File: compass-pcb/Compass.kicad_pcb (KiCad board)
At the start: 2 copper layers, 18 parts

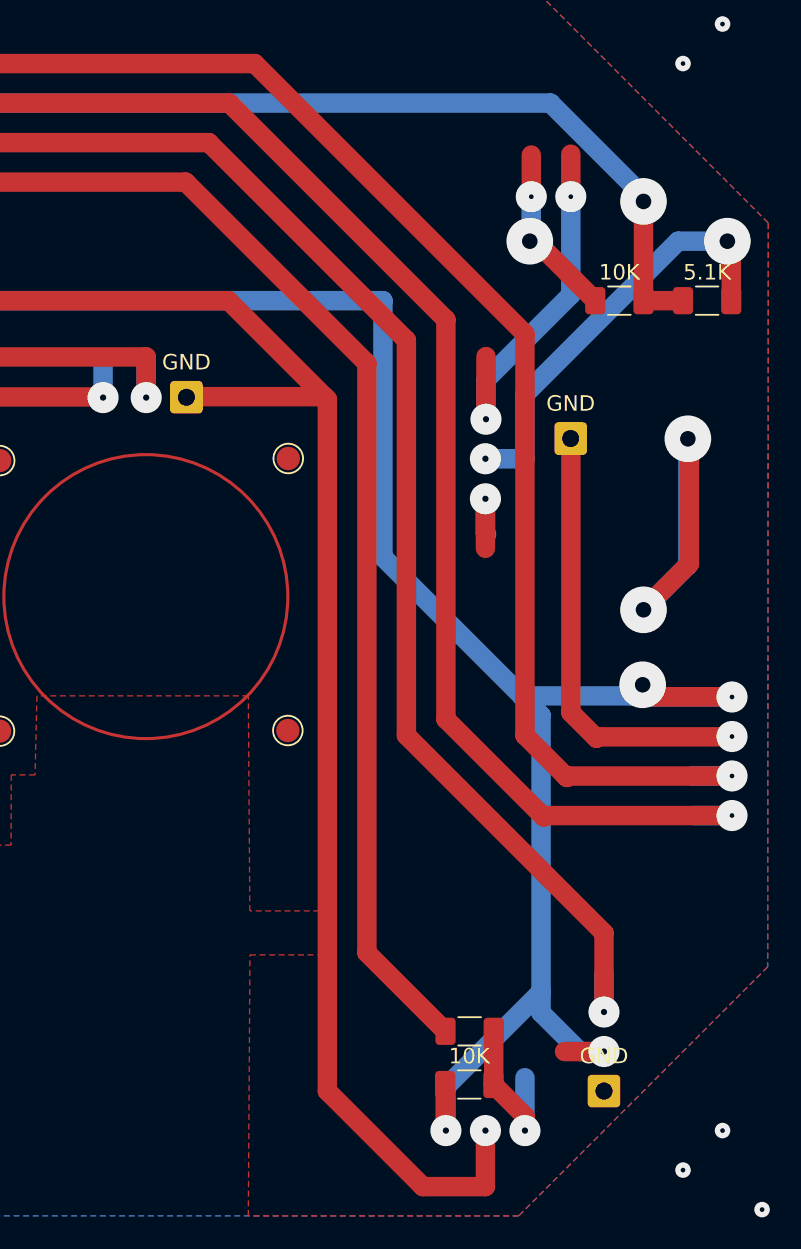
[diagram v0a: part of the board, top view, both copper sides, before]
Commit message: moving jumpers for more space
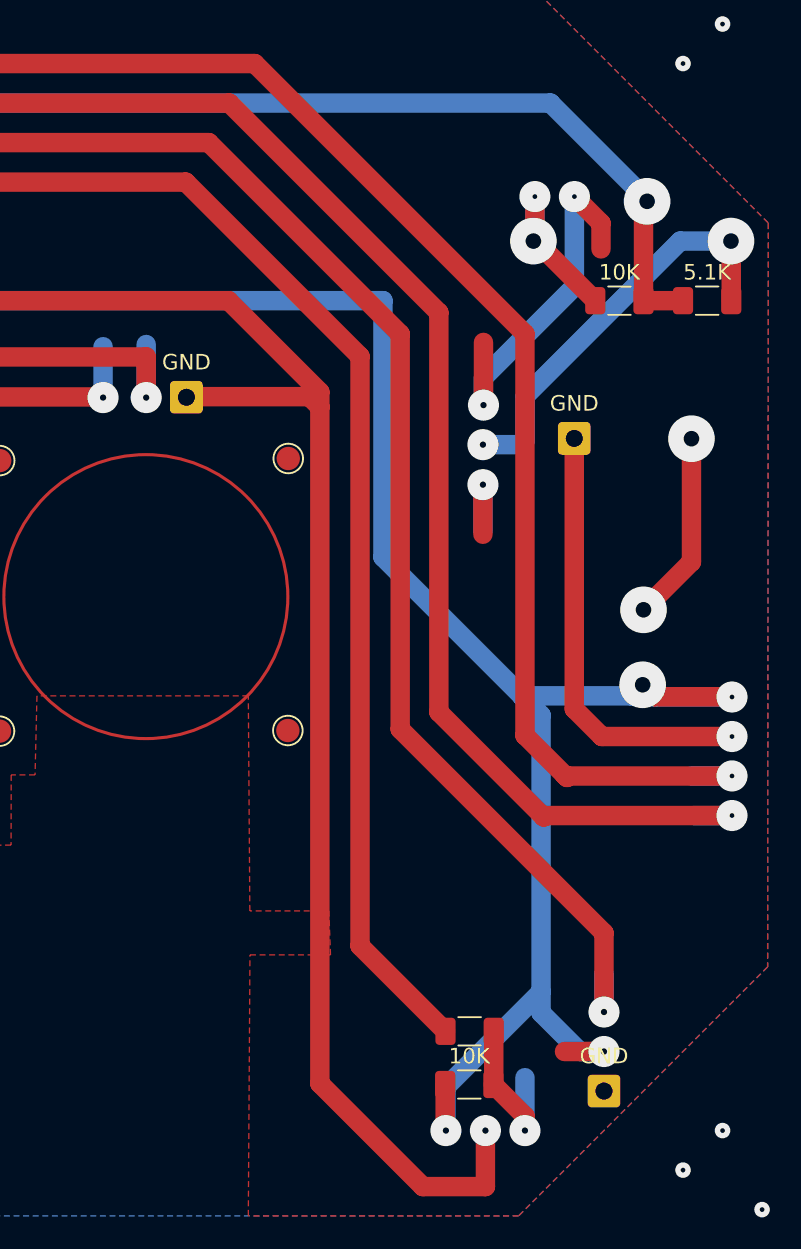
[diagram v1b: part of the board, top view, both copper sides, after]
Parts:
- moved GND 0.23 mm to (174.9, 83.8)
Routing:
- net (no net): track 1122.2 -> 1116.1 mm

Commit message: polishing
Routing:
- net (no net): track 1116.1 -> 1124.7 mm
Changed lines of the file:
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@@
   (segment (start 162.56 91.44) (end 162.56 74.958533) (width 1.25) (layer "B.Cu") (net 0))
   (segment (start 174.864516 68.268417) (end 174.864516 74.055484) (width 1.25) (layer "B.Cu") (net 0))
+  (segment (start 128.505445 100.278533) (end 130.516888 100.278533) (width 1.25) (layer "B.Cu") (net 0))
   (segment (start 108.787292 77.48937) (end 111.429859 77.48937) (width 1.25) (layer "B.Cu") (net 0))
   (segment (start 179.250238 99.646343) (end 178.538048 100.358533) (width 1.25) (layer "B.Cu") (net 0))
@@
   (segment (start 179.537067 68.472794) (end 173.322806 62.258533) (width 1.25) (layer "B.Cu") (net 0))
   (segment (start 108.85939 87.721468) (end 108.787292 87.64937) (width 1.25) (layer "B.Cu") (net 0))
+  (segment (start 168.984917 86.784602) (end 168.984917 89.944634) (width 1.25) (layer "B.Cu") (net 0))
   (segment (start 116.84 85.118533) (end 124.013168 85.118533) (width 1.25) (layer "B.Cu") (net 0))
   (segment (start 180.034912 100.431017) (end 184.993201 100.431017) (width 1.25) (layer "B.Cu") (net 0))
   (segment (start 121.473069 105.420339) (end 124.029538 105.420339) (width 1.25) (layer "B.Cu") (net 0))
   (segment (start 111.312994 79.999811) (end 108.816851 79.999811) (width 1.25) (layer "B.Cu") (net 0))
-  (segment (start 168.984917 86.784602) (end 168.984917 89.76346) (width 1.25) (layer "B.Cu") (net 0))
   (segment (start 168.984917 84.211715) (end 168.984917 83.90582) (width 1.25) (layer "B.Cu") (net 0))
   (segment (start 178.538048 100.358533) (end 171.478533 100.358533) (width 1.25) (layer "B.Cu") (net 0))
   (segment (start 108.818788 92.760866) (end 108.787292 92.72937) (width 1.25) (layer "B.Cu") (net 0))
+  (segment (start 128.505445 97.778533) (end 130.657549 97.778533) (width 1.25) (layer "B.Cu") (net 0))
   (segment (start 179.537067 68.573184) (end 179.537067 68.472794) (width 1.25) (layer "B.Cu") (net 0))
   (segment (start 171.69707 81.098057) (end 171.69707 83.966348) (width 1.25) (layer "B.Cu") (net 0))
@@
   (segment (start 123.96871 90.241167) (end 124.053119 90.156758) (width 1.25) (layer "B.Cu") (net 0))
   (segment (start 123.970383 110.561318) (end 124.013168 110.518533) (width 1.25) (layer "B.Cu") (net 0))
+  (segment (start 128.505445 102.898533) (end 130.678141 102.898533) (width 1.25) (layer "B.Cu") (net 0))
   (segment (start 166.605445 125.494555) (end 172.72 119.38) (width 1.25) (layer "B.Cu") (net 0))
   (segment (start 171.478533 100.358533) (end 172.72 101.6) (width 1.25) (layer "B.Cu") (net 0))
@@
   (segment (start 111.443824 100.34937) (end 111.453019 100.340175) (width 1.25) (layer "B.Cu") (net 0))
   (segment (start 179.250238 99.646343) (end 180.034912 100.431017) (width 1.25) (layer "B.Cu") (net 0))
+  (segment (start 128.505445 95.278533) (end 130.598297 95.278533) (width 1.25) (layer "B.Cu") (net 0))
   (segment (start 108.816851 82.539811) (end 108.787292 82.56937) (width 1.25) (layer "B.Cu") (net 0))
   (segment (start 124.053119 87.616758) (end 121.324313 87.616758) (width 1.25) (layer "B.Cu") (net 0))

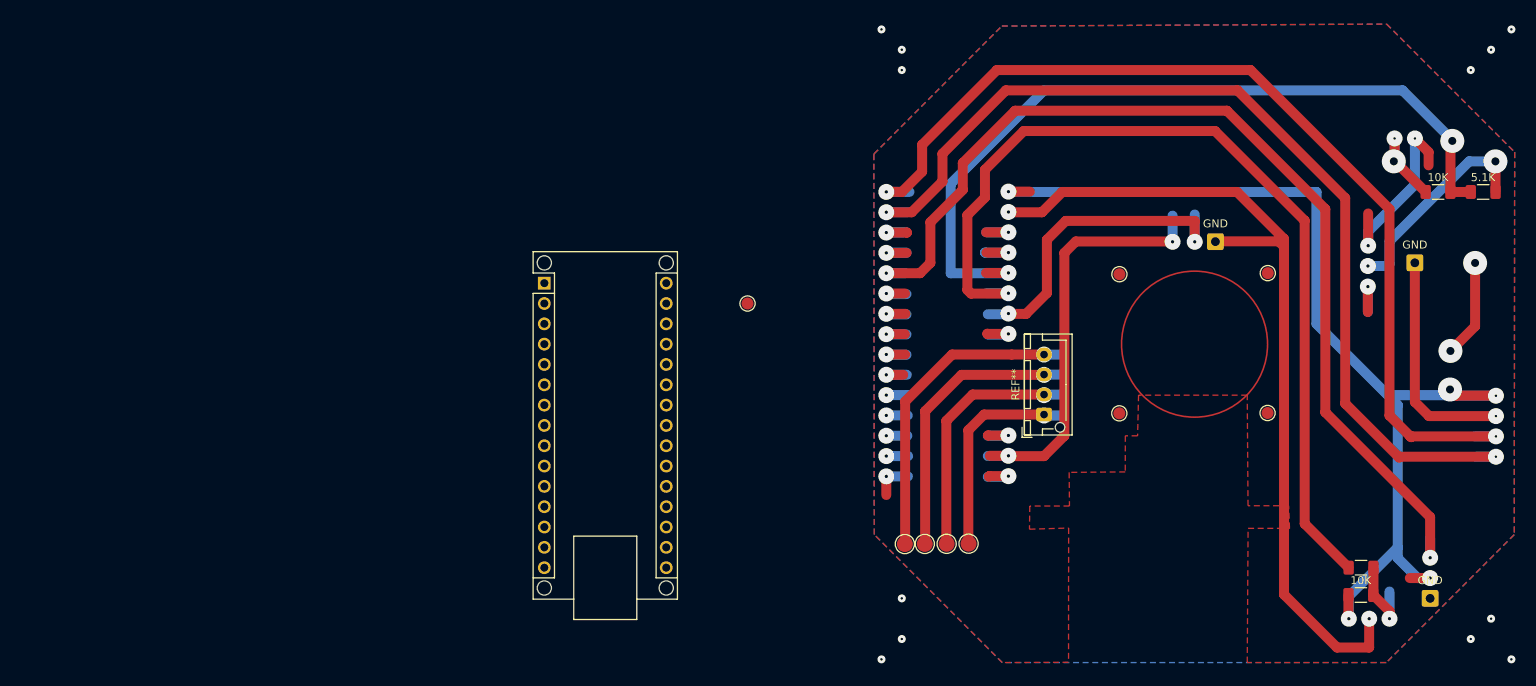
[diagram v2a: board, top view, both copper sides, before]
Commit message: moving main switch to the board
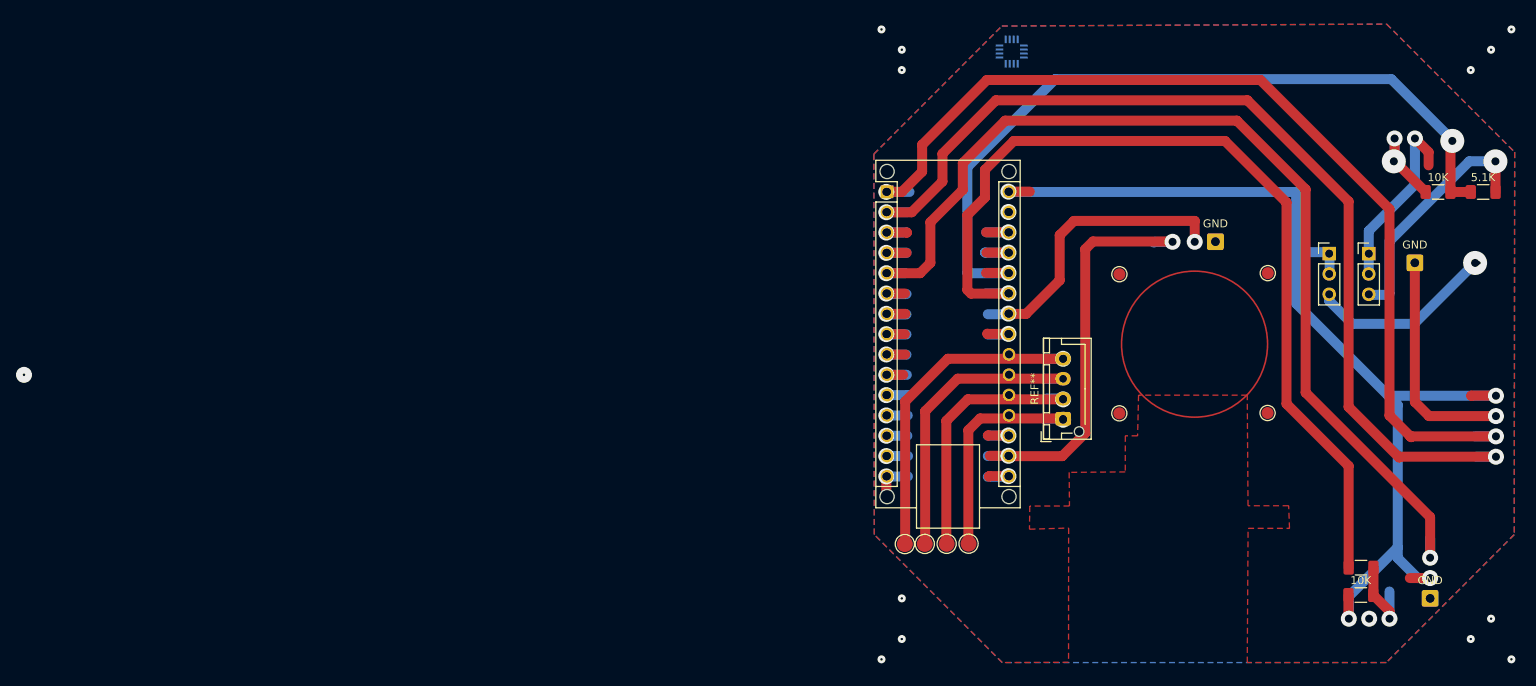
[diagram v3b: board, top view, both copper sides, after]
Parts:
- removed the REF** at (91.4, 88.9)
- added  : main switch, Connector_PinHeader_2.54mm:PinHeader_1x03_P2.54mm_Vertical, F.Cu at (164.2, 82.7)
- added  : battery switch, Connector_PinHeader_2.54mm:PinHeader_1x03_P2.54mm_Vertical, F.Cu at (169.1, 82.7)
- added REF**: HMC5883L, HMC5883L:HMC5883L_EXTENDED, B.Cu at (124.5, 57.4)
- moved REF** 44.3 mm to (108.9, 74.9)
- moved REF** 2.44 mm to (130.9, 103.3)
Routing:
- net GND: track 137.2 -> 29.0 mm
- net (no net): track 1124.7 -> 1132.9 mm, vias 61 -> 57
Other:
- board text removed: "Battery jumper"

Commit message: moving charger to the board
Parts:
- removed the GND at (149.9, 81.2)
- added  : Encoder, Connector_PinHeader_2.54mm:PinHeader_1x03_P2.54mm_Vertical, F.Cu at (149.9, 81.3)
- added REF**: Charger, Connector_JST:JST_XH_B2B-XH-A_1x02_P2.50mm_Vertical, F.Cu at (130.9, 88.6)
- added REF**: Charger cable, Connector_PinHeader_2.54mm:PinHeader_1x02_P2.54mm_Vertical, F.Cu at (153.7, 81.3)
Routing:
- net (no net): track 1132.9 -> 1216.9 mm, vias 57 -> 54
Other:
- board text removed: "Encoder"

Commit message: polishing the pcb
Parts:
- removed the REF** at (156.4, 102.6)
- removed the REF** at (137.9, 85.2)
- removed the REF** at (137.9, 102.6)
- removed the REF** at (156.5, 85.1)
- added GND: , Connector_Wire:SolderWire-0.5sqmm_1x01_D0.9mm_OD2.1mm, F.Cu at (137.9, 102.6)
- added GND: , Connector_Wire:SolderWire-0.5sqmm_1x01_D0.9mm_OD2.1mm, F.Cu at (156.4, 102.6)
- added GND: , Connector_Wire:SolderWire-0.5sqmm_1x01_D0.9mm_OD2.1mm, F.Cu at (156.5, 85.1)
- added GND: , Connector_Wire:SolderWire-0.5sqmm_1x01_D0.9mm_OD2.1mm, F.Cu at (137.9, 85.2)
- moved REF** 0.50 mm to (154.2, 81.3)
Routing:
- net (no net): track 1216.9 -> 1212.7 mm, vias 54 -> 51

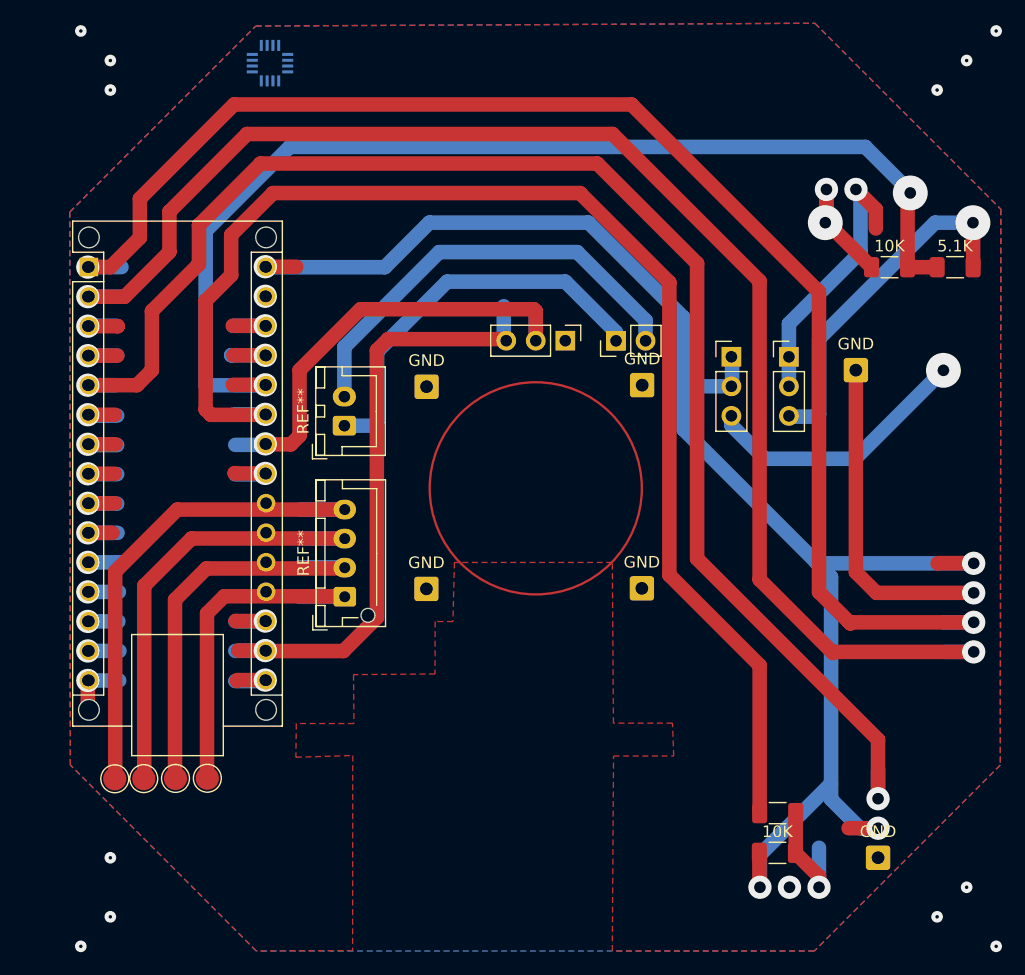
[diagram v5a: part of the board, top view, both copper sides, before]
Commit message: copy main shape to back side
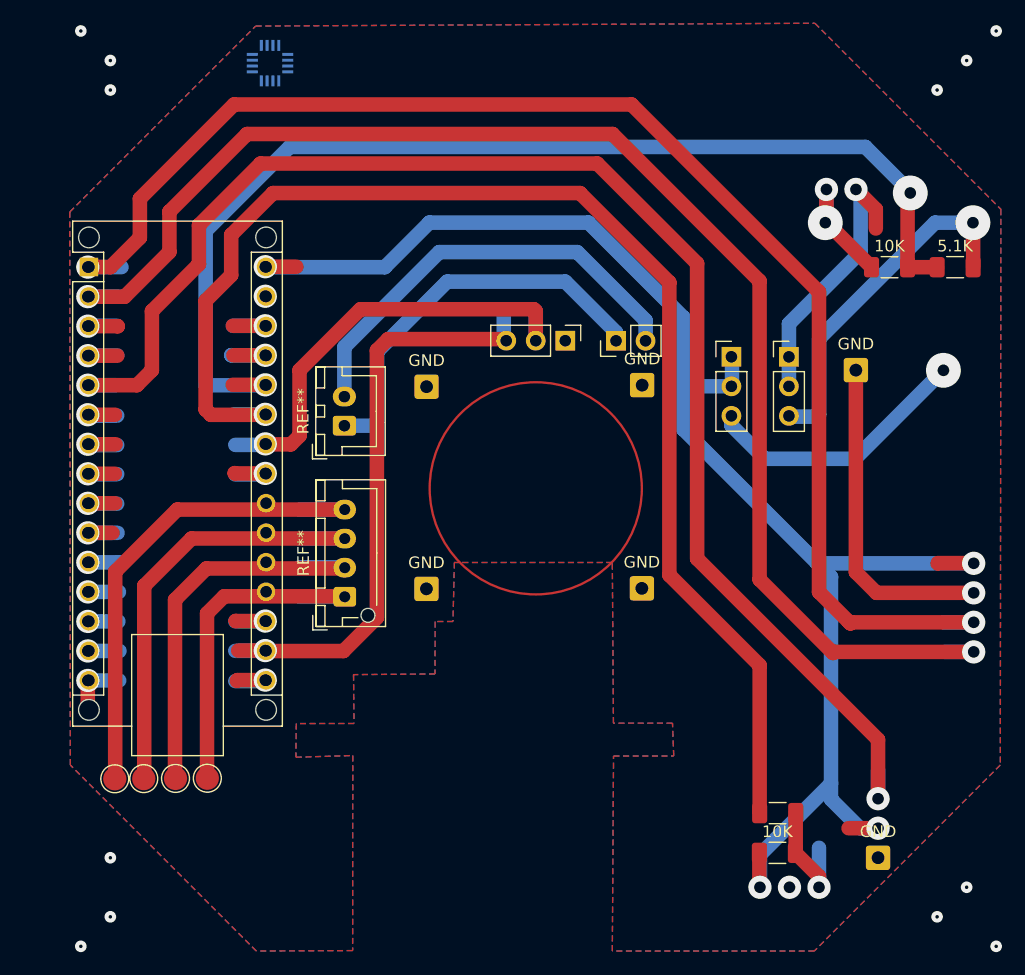
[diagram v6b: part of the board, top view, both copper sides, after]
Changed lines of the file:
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@@
   (segment (start 175.676928 64.612655) (end 126.151323 64.612655) (width 1.25) (layer "B.Cu") (net 0))
   (segment (start 179.537067 68.573184) (end 179.537067 68.472794) (width 1.25) (layer "B.Cu") (net 0))
-  (segment (start 144.570556 81.187222) (end 144.570556 78.315724) (width 1.25) (layer "B.Cu") (net 0))
+  (segment (start 144.570556 81.187222) (end 144.570556 78.74) (width 1.25) (layer "B.Cu") (net 0))
   (segment (start 149.86 76.2) (end 154.225254 80.565254) (width 1.25) (layer "B.Cu") (net 0))
   (segment (start 127 103.308212) (end 130.88831 103.308212) (width 1.25) (layer "B.Cu") (net 0))
@@
   (via (at 124.053119 77.456758) (size 2) (drill 1) (layers "F.Cu" "B.Cu") (net 1))
   (segment (start 184.883296 102.861112) (end 184.993201 102.971017) (width 1.25) (layer "B.Cu") (net 1))
-  (zone (net 1) (net_name "GND") (layer "F.Cu") (hatch edge 0.5)
+  (zone (net 1) (net_name "GND") (layers "F&B.Cu") (hatch edge 0.5)
     (connect_pads (clearance 1.25))
     (min_thickness 0.5) (filled_areas_thickness no)
@@
       )
     )
-  )
-  (zone (net 1) (net_name "GND") (layer "B.Cu") (hatch edge 0.5)
-    (connect_pads (clearance 1.25))
-    (min_thickness 0.5) (filled_areas_thickness no)
-    (fill yes (thermal_gap 1) (thermal_bridge_width 0.7) (island_removal_mode 1) (island_area_min 10))
-    (polygon
-      (pts
-        (xy 123.281198 133.78172)
-        (xy 107.281198 117.78172)
-        (xy 107.233111 70.214506)
-        (xy 123.233111 54.214506)
-        (xy 171.330346 53.973539)
-        (xy 187.330346 69.973539)
-        (xy 187.282258 117.78172)
-        (xy 171.282258 133.78172)
-      )
-    )

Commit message: polishing, adding border
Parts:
- removed the GND at (137.9, 102.6)
- removed the GND at (156.4, 102.6)
- removed the GND at (156.5, 85.1)
- removed the REF** at (130.9, 103.3)
- removed the REF** at (108.9, 74.9)
- added ?: GPS, Connector_PinHeader_2.54mm:PinHeader_1x04_P2.54mm_Vertical, F.Cu at (185.0, 100.4)
- added GND: , Connector_Wire:SolderWire-0.5sqmm_1x01_D0.9mm_OD2.1mm, F.Cu at (156.4, 102.8)
- added GND: , Connector_Wire:SolderWire-0.5sqmm_1x01_D0.9mm_OD2.1mm, F.Cu at (137.9, 102.8)
- added GND: , Connector_Wire:SolderWire-0.5sqmm_1x01_D0.9mm_OD2.1mm, F.Cu at (147.3, 94.0)
- added GND: , Connector_Wire:SolderWire-0.5sqmm_1x01_D0.9mm_OD2.1mm, F.Cu at (156.4, 85.2)
- added REF**: Arduino_Nano, Module:Arduino_Nano, F.Cu at (108.9, 75.0)
- added REF**: JST_XH_B4B-XH-A_1x04_P2.50mm_Vertical, Connector_JST:JST_XH_B4B-XH-A_1x04_P2.50mm_Vertical, F.Cu at (130.7, 103.4)
-  : value main switch -> main
-  : value battery switch -> battery
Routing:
- net (no net): track 1212.3 -> 1234.6 mm, vias 51 -> 23
- net GND: track 29.0 -> 34.4 mm, vias 3 -> 1
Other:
- board outline added: 81.3 x 81.7 mm
- board text added: "Alignment anchors: 1) print stencil 2) drill alignment holes (outside of corners) 3) align back side stencil by these holes (use light)"
- board text removed: "Alignment anchors: 1) print stencil 2) drill these holes 3) align back side stencil by these holes"
- board text removed: "GPS"
